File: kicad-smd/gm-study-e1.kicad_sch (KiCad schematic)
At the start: 12 parts

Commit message: file updates
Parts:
- R29: value 160 -> 180
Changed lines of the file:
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@@
   (symbol (lib_id "Device:R_Small") (at 69.85 179.07 90) (unit 1)
     (in_bom yes) (on_board yes)
-    (property "Reference" "R29" (id 0) (at 69.85 176.53 90))
-    (property "Value" "160" (id 1) (at 69.85 179.07 90))
+    (property "Reference" "R29" (id 0) (at 66.04 177.8 90))
+    (property "Value" "180" (id 1) (at 74.93 177.8 90))
     (property "Footprint" "Resistor_SMD:R_0402_1005Metric" (id 2) (at 69.85 179.07 0)
       (effects (font (size 1.27 1.27)) hide)
@@
       (reference "J1") (unit 1) (value "Conn_01x16") (footprint "Connector_PinHeader_2.54mm:PinHeader_1x16_P2.54mm_Vertical")
     )
-    (path "/c2ce2db8-0c6b-4dd5-bb07-3b39fea01243/cdd55ec0-a32d-4e52-b010-c9945ae875a9"
-      (reference "JP1") (unit 1) (value "Jumper") (footprint "Connector_PinHeader_2.54mm:PinHeader_1x02_P2.54mm_Vertical")
-    )
     (path "/55aa19aa-4e00-4e71-83a9-51c462d9a2c0/f9f2c2ff-1c55-49dc-9160-b1239897bb85"
       (reference "L1") (unit 1) (value "4.7uH") (footprint "Inductor_SMD:L_0603_1608Metric")
@@
     )
     (path "/55aa19aa-4e00-4e71-83a9-51c462d9a2c0/99f089fa-5203-42f4-bc84-a57394ca1da4"
-      (reference "R11") (unit 1) (value "160") (footprint "Resistor_SMD:R_0402_1005Metric")
+      (reference "R11") (unit 1) (value "200") (footprint "Resistor_SMD:R_0402_1005Metric")
     )
     (path "/55aa19aa-4e00-4e71-83a9-51c462d9a2c0/387ac8c6-0d9a-4f7a-89c9-2f3d22ae6a2f"
-      (reference "R12") (unit 1) (value "160") (footprint "Resistor_SMD:R_0402_1005Metric")
+      (reference "R12") (unit 1) (value "200") (footprint "Resistor_SMD:R_0402_1005Metric")
     )
     (path "/55aa19aa-4e00-4e71-83a9-51c462d9a2c0/b07b1386-8d41-496d-b474-bc3b02454877"
-      (reference "R13") (unit 1) (value "160") (footprint "Resistor_SMD:R_0402_1005Metric")
+      (reference "R13") (unit 1) (value "200") (footprint "Resistor_SMD:R_0402_1005Metric")
     )
     (path "/55aa19aa-4e00-4e71-83a9-51c462d9a2c0/a6ea8723-6c9a-4e69-92a4-16d4b0a51c42"
-      (reference "R14") (unit 1) (value "160") (footprint "Resistor_SMD:R_0402_1005Metric")
+      (reference "R14") (unit 1) (value "200") (footprint "Resistor_SMD:R_0402_1005Metric")
     )
     (path "/55aa19aa-4e00-4e71-83a9-51c462d9a2c0/6d485ad6-ed5e-4b11-8f40-020df7b546af"
-      (reference "R15") (unit 1) (value "160") (footprint "Resistor_SMD:R_0402_1005Metric")
+      (reference "R15") (unit 1) (value "200") (footprint "Resistor_SMD:R_0402_1005Metric")
     )
     (path "/55aa19aa-4e00-4e71-83a9-51c462d9a2c0/a3d7eaec-ebf2-4474-bf7f-990caeb3ca18"
-      (reference "R16") (unit 1) (value "160") (footprint "Resistor_SMD:R_0402_1005Metric")
+      (reference "R16") (unit 1) (value "200") (footprint "Resistor_SMD:R_0402_1005Metric")
     )
     (path "/55aa19aa-4e00-4e71-83a9-51c462d9a2c0/6056104d-d3e9-4af8-bd93-bcd9d898d970"
-      (reference "R17") (unit 1) (value "160") (footprint "Resistor_SMD:R_0402_1005Metric")
+      (reference "R17") (unit 1) (value "200") (footprint "Resistor_SMD:R_0402_1005Metric")
     )
     (path "/55aa19aa-4e00-4e71-83a9-51c462d9a2c0/c9b1dbe6-92df-42ce-8804-c4378d3ae055"
-      (reference "R18") (unit 1) (value "160") (footprint "Resistor_SMD:R_0402_1005Metric")
+      (reference "R18") (unit 1) (value "200") (footprint "Resistor_SMD:R_0402_1005Metric")
     )
     (path "/55aa19aa-4e00-4e71-83a9-51c462d9a2c0/226598e4-efa8-428b-9a17-6d7b750837c2"
-      (reference "R19") (unit 1) (value "160") (footprint "Resistor_SMD:R_0402_1005Metric")
+      (reference "R19") (unit 1) (value "200") (footprint "Resistor_SMD:R_0402_1005Metric")
     )
     (path "/55aa19aa-4e00-4e71-83a9-51c462d9a2c0/fcf81bc3-fa75-43a3-ae0a-d6dad0120be0"
-      (reference "R20") (unit 1) (value "160") (footprint "Resistor_SMD:R_0402_1005Metric")
+      (reference "R20") (unit 1) (value "200") (footprint "Resistor_SMD:R_0402_1005Metric")
     )
     (path "/c2ce2db8-0c6b-4dd5-bb07-3b39fea01243/a17e37ea-ea68-46af-adf7-a4b8b99a41a3"
@@
     )
     (path "/cec84998-35f9-4381-a25e-1a8f72cdd9f2"
-      (reference "R29") (unit 1) (value "160") (footprint "Resistor_SMD:R_0402_1005Metric")
+      (reference "R29") (unit 1) (value "180") (footprint "Resistor_SMD:R_0402_1005Metric")
     )
     (path "/55aa19aa-4e00-4e71-83a9-51c462d9a2c0/c642ed85-95b4-496b-b07e-89d16238bb9e"
-      (reference "R30") (unit 1) (value "160") (footprint "Resistor_THT:R_Axial_DIN0204_L3.6mm_D1.6mm_P5.08mm_Horizontal")
+      (reference "R30") (unit 1) (value "100") (footprint "Resistor_THT:R_Axial_DIN0204_L3.6mm_D1.6mm_P5.08mm_Horizontal")
     )
     (path "/55aa19aa-4e00-4e71-83a9-51c462d9a2c0/0d340f53-7f13-4000-9a47-40d819c1f061"
-      (reference "RA1") (unit 1) (value "180") (footprint "FM4DD:R_Array_Convex_4x0603")
+      (reference "RA1") (unit 1) (value "200") (footprint "FM4DD:R_Array_Convex_4x0603")
     )
     (path "/55aa19aa-4e00-4e71-83a9-51c462d9a2c0/d4ac9aae-675a-45d3-adb4-1d4066651023"
-      (reference "RA2") (unit 1) (value "180") (footprint "FM4DD:R_Array_Convex_4x0603")
+      (reference "RA2") (unit 1) (value "200") (footprint "FM4DD:R_Array_Convex_4x0603")
     )
     (path "/55aa19aa-4e00-4e71-83a9-51c462d9a2c0/c6773a7c-120a-4429-9093-6f46ef721284"
-      (reference "RA3") (unit 1) (value "180") (footprint "FM4DD:R_Array_Convex_4x0603")
+      (reference "RA3") (unit 1) (value "200") (footprint "FM4DD:R_Array_Convex_4x0603")
     )
     (path "/55aa19aa-4e00-4e71-83a9-51c462d9a2c0/88fa644b-f537-4f86-b47f-1c0239ccf517"
-      (reference "RA4") (unit 1) (value "180") (footprint "FM4DD:R_Array_Convex_4x0603")
+      (reference "RA4") (unit 1) (value "200") (footprint "FM4DD:R_Array_Convex_4x0603")
     )
     (path "/55aa19aa-4e00-4e71-83a9-51c462d9a2c0/242575ab-9dbb-40d9-9482-e100c97a1309"
-      (reference "RA5") (unit 1) (value "180") (footprint "FM4DD:R_Array_Convex_4x0603")
+      (reference "RA5") (unit 1) (value "200") (footprint "FM4DD:R_Array_Convex_4x0603")
     )
     (path "/55aa19aa-4e00-4e71-83a9-51c462d9a2c0/a411fe1f-5974-46f7-95c9-711c4664d43a"
-      (reference "RA6") (unit 1) (value "180") (footprint "FM4DD:R_Array_Convex_4x0603")
+      (reference "RA6") (unit 1) (value "200") (footprint "FM4DD:R_Array_Convex_4x0603")
     )
     (path "/55aa19aa-4e00-4e71-83a9-51c462d9a2c0/752749e3-40f3-4294-9df9-6d74cd930317"
-      (reference "RA7") (unit 1) (value "180") (footprint "FM4DD:R_Array_Convex_4x0603")
+      (reference "RA7") (unit 1) (value "200") (footprint "FM4DD:R_Array_Convex_4x0603")
     )
     (path "/55aa19aa-4e00-4e71-83a9-51c462d9a2c0/d0ab2d9a-ac21-4f56-921b-3541b1a0aac4"
-      (reference "RA8") (unit 1) (value "180") (footprint "FM4DD:R_Array_Convex_4x0603")
+      (reference "RA8") (unit 1) (value "200") (footprint "FM4DD:R_Array_Convex_4x0603")
     )
     (path "/55aa19aa-4e00-4e71-83a9-51c462d9a2c0/4df9936f-261e-4801-9d59-a70e7f13059c"
-      (reference "RA9") (unit 1) (value "180") (footprint "FM4DD:R_Array_Convex_4x0603")
+      (reference "RA9") (unit 1) (value "200") (footprint "FM4DD:R_Array_Convex_4x0603")
     )
     (path "/55aa19aa-4e00-4e71-83a9-51c462d9a2c0/126f935c-c777-4aa1-b65a-83756ab5d5b1"
-      (reference "RA10") (unit 1) (value "180") (footprint "FM4DD:R_Array_Convex_4x0603")
+      (reference "RA10") (unit 1) (value "200") (footprint "FM4DD:R_Array_Convex_4x0603")
     )
     (path "/55aa19aa-4e00-4e71-83a9-51c462d9a2c0/bec0f4a9-a927-4c92-90e3-e61bf94517bd"
-      (reference "RA11") (unit 1) (value "180") (footprint "FM4DD:R_Array_Convex_4x0603")
+      (reference "RA11") (unit 1) (value "200") (footprint "FM4DD:R_Array_Convex_4x0603")
     )
     (path "/55aa19aa-4e00-4e71-83a9-51c462d9a2c0/ed21ca10-af38-482a-b148-473c4f4f53aa"
-      (reference "RA12") (unit 1) (value "180") (footprint "FM4DD:R_Array_Convex_4x0603")
+      (reference "RA12") (unit 1) (value "200") (footprint "FM4DD:R_Array_Convex_4x0603")
     )
     (path "/39ada7b3-8f98-4dc3-955f-51f06547ccfa"

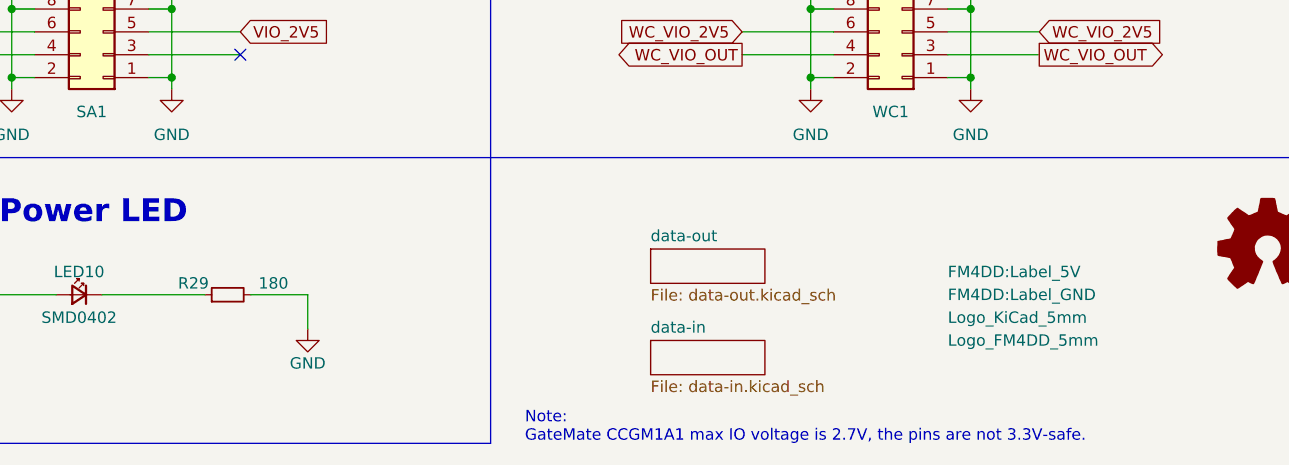
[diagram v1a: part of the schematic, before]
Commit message: New SMB PCB v1.1 updates J1 level translation IC
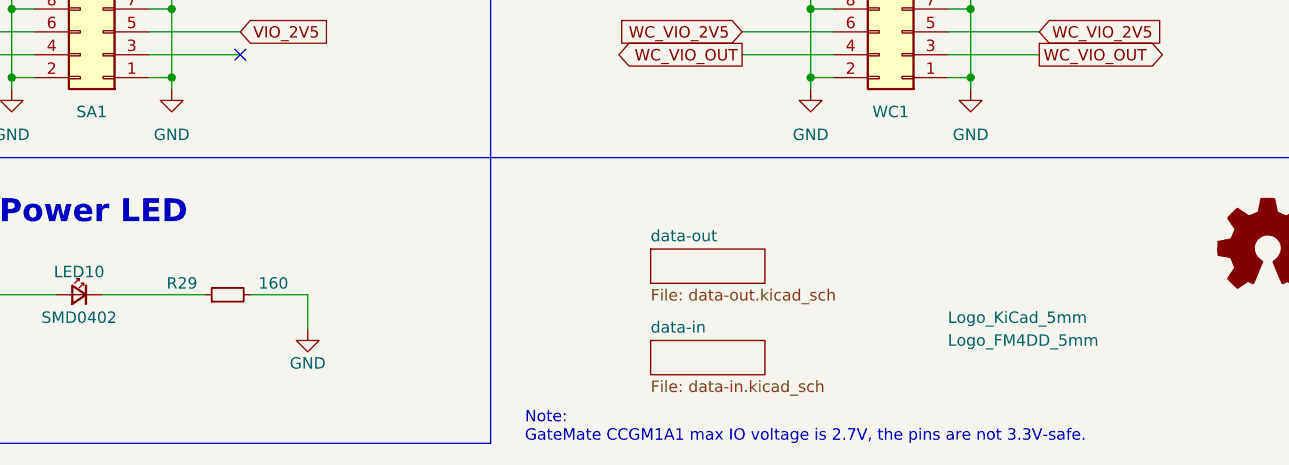
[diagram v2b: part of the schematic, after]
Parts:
- LED10: footprint FM4DD:LED_0402_FPGA -> FM4DD:LED_0402_no_frame
- R29: value 180 -> 160
